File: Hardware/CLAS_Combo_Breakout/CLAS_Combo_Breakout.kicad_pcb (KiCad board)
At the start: 4 copper layers, 60 x 60 mm, 87 parts, among them J1 USB_C_Receptacle_USB2.0, J2 ZED, J3 NEO, J4 USB_C_Receptacle_USB2.0, J5 Conn_Coaxial, Q1 DSS20200, U1 USBLC6-2P6, U2 ZED-F9P, U3 NEO-D9C-00B, U4 USBLC6-2P6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

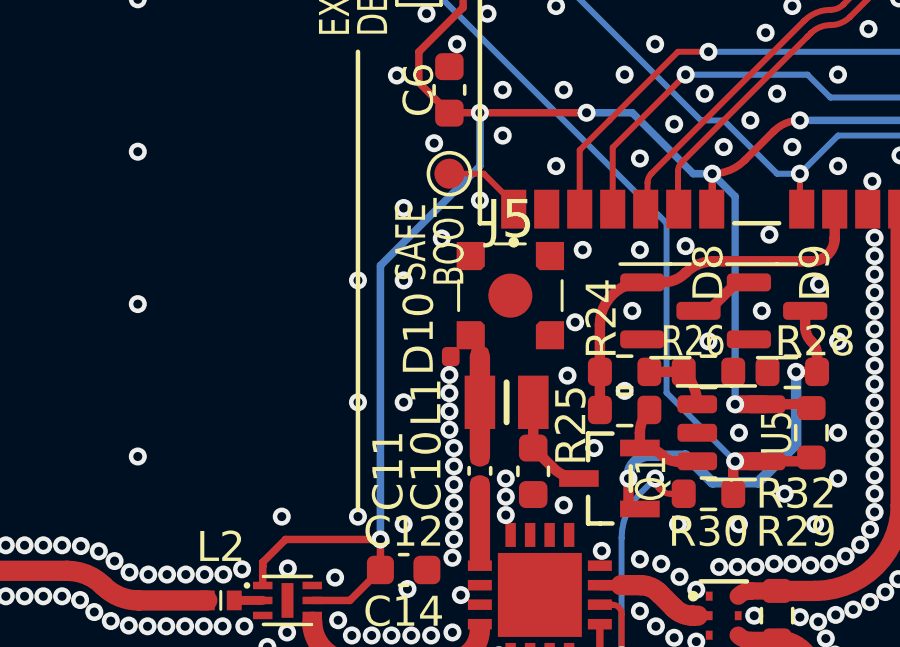
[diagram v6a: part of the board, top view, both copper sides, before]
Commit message: インダクタを変更　フットプリントを追加
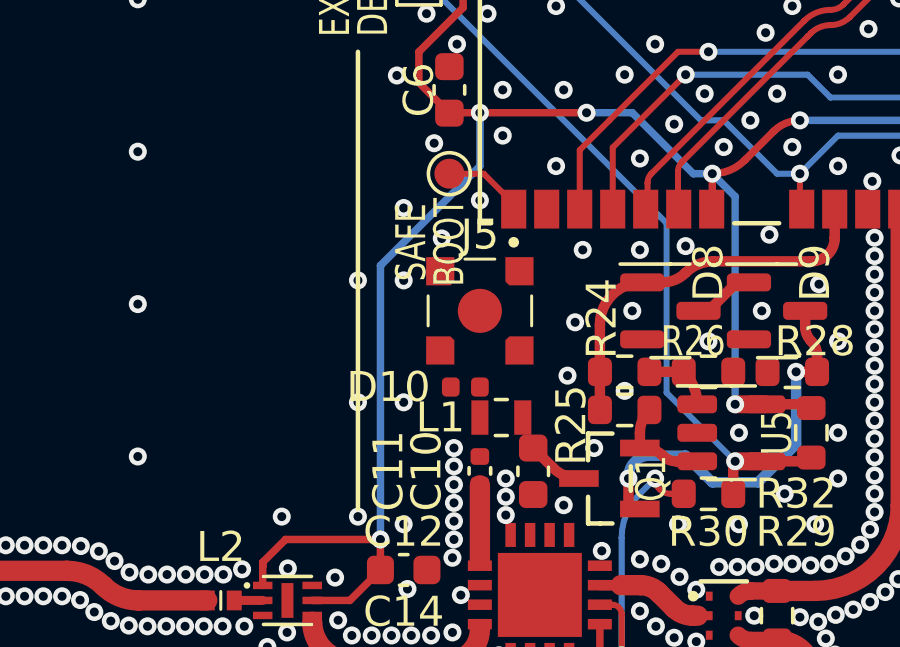
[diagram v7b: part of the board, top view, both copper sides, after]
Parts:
- L1: value LQW2BANR12J00L -> LQW18ANR12G8ZD; footprint LQW2BANR12J00L:LQW2BANR12J00L -> LQW18ANR12G8ZD:LQW18ANR12G8ZD
- moved J5 1.14 mm to (135.1, 111.3)
- moved D10 1.02 mm to (134.6, 113.9)
- moved L1 0.54 mm to (135.8, 114.9)
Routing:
- net Net-(C11-Pad1): track 3.33 -> 0.00 mm
- net Net-(C10-Pad2): track 3.41 -> 1.89 mm
- net GND: vias 536 -> 532

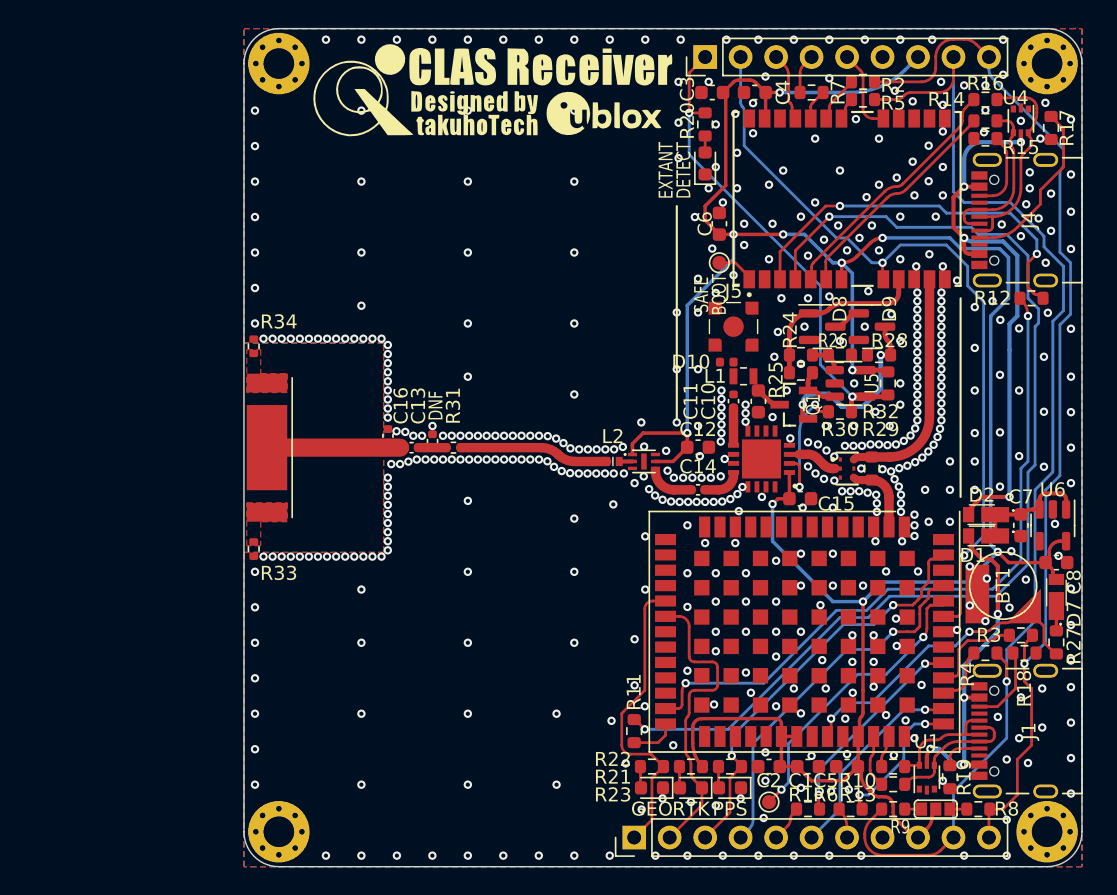
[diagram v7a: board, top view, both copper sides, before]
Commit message: 外部アンテナの伝送路を整備
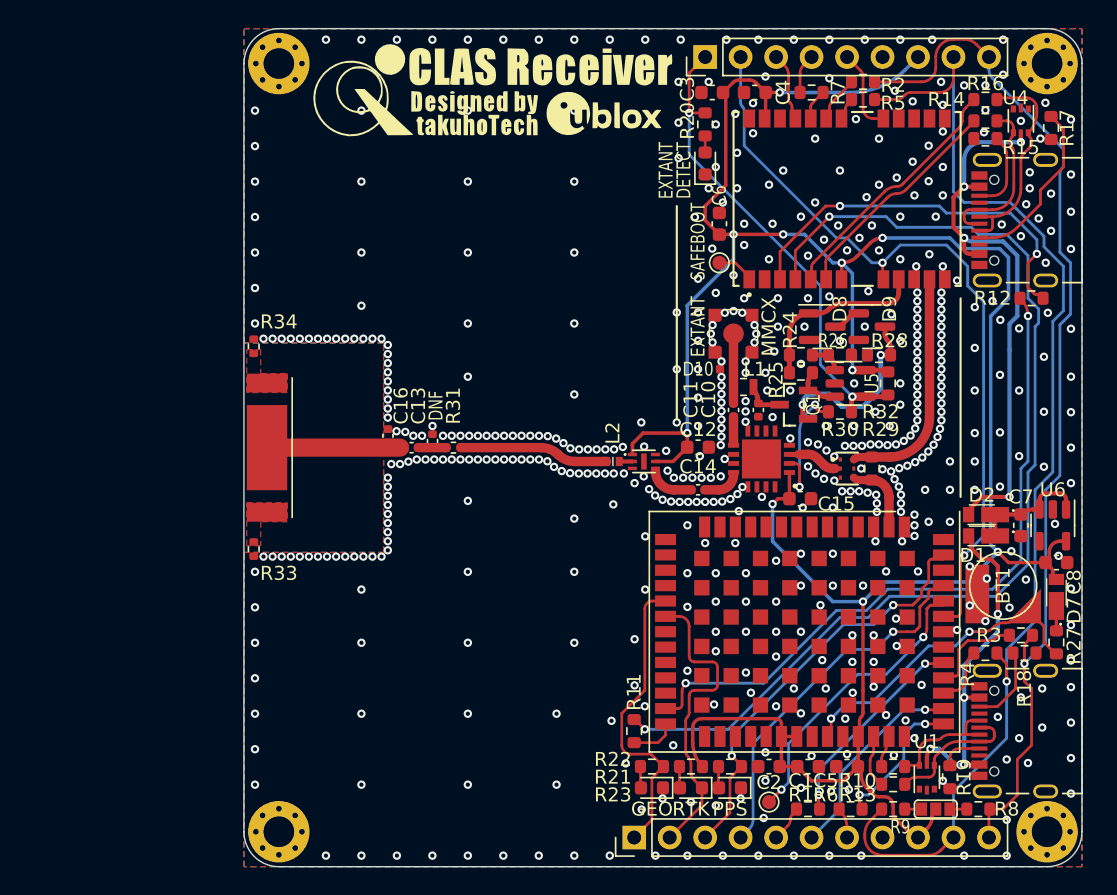
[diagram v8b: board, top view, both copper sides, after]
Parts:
- C10: footprint Capacitor_SMD:C_0603_1608Metric -> Capacitor_SMD:C_0402_1005Metric
- moved L1 0.76 mm to (135.8, 115.7)
- moved C11 0.64 mm to (135.1, 117.3)
- moved C10 0.62 mm to (136.8, 117.3)
- moved D10 0.51 mm to (134.6, 114.4)
- moved J5 0.51 mm to (135.1, 111.8)
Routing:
- net Net-(C11-Pad1): track 0.00 -> 4.98 mm
- net Net-(C10-Pad2): track 1.89 -> 2.82 mm
- net Net-(C11-Pad2): track 2.49 -> 1.86 mm
- net GND: vias 532 -> 551
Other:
- board text added: "MMCX"
- board text added: "SAFEBOOT"
- board text removed: "BOOT"
- board text removed: "SAFE"
